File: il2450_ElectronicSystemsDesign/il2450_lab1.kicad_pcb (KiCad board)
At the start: 2 copper layers, 33 x 31.5 mm, 76 parts, among them P1 USB_OTG, P2 Spy-Bi-Wire, P3 UART, U1 LM1117-3.3, U2 MSP430G2553IPW20, U3 TMP101NA/250, Y1 Crystal

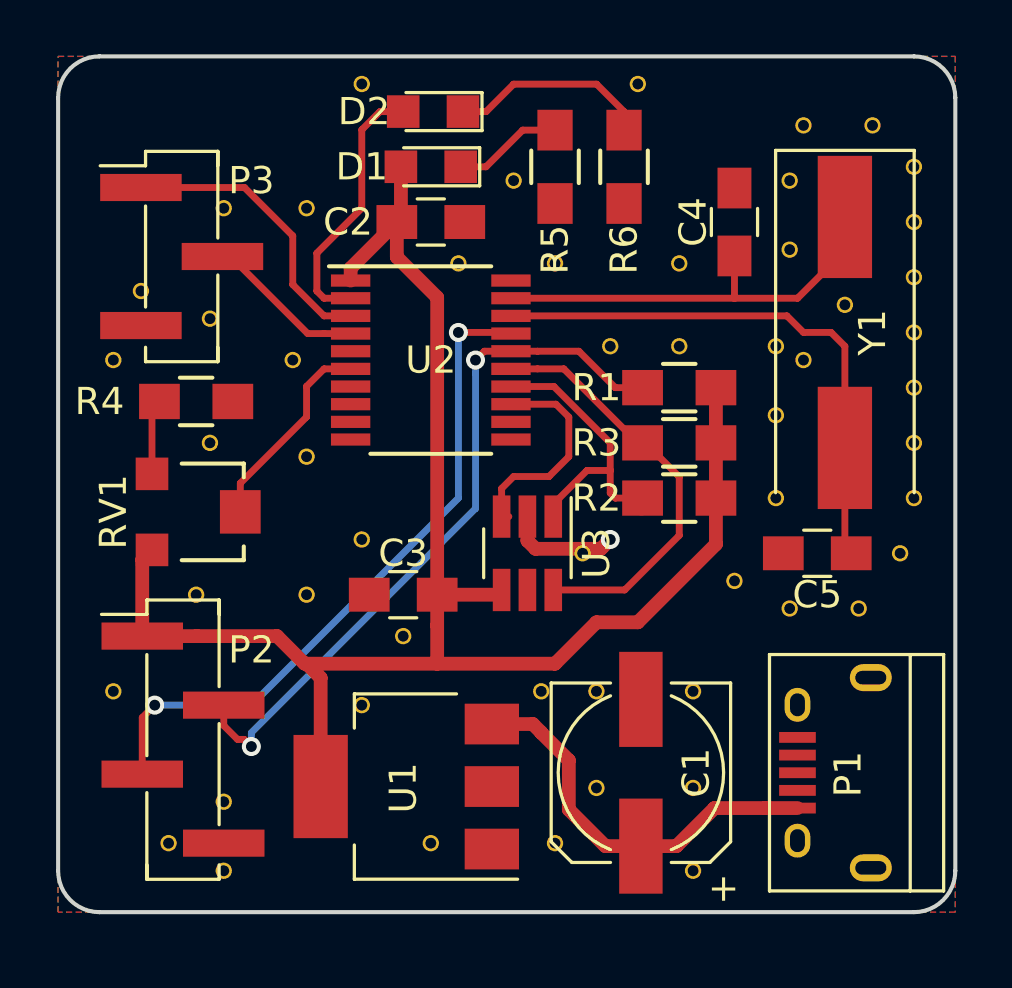
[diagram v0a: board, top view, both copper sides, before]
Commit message: Added board dimensions
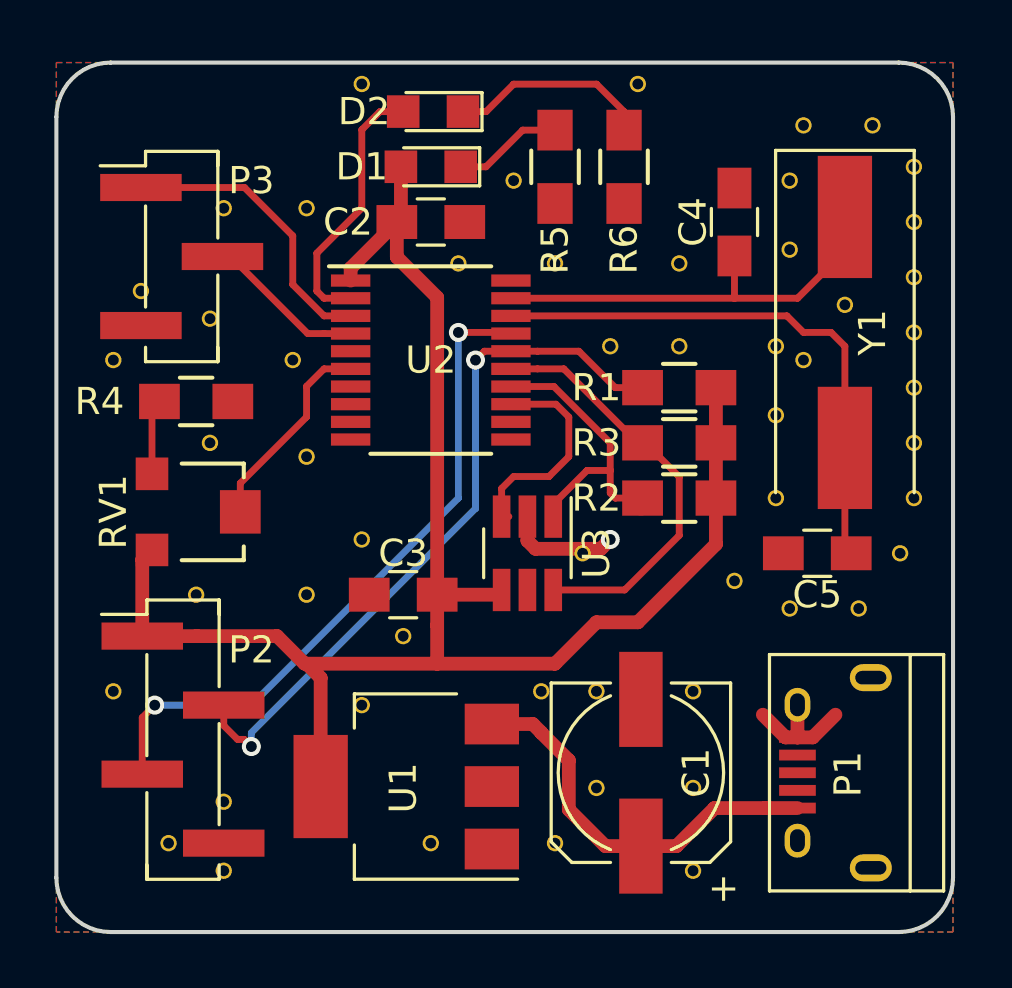
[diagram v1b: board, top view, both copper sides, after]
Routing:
- net GND: track 4.20 -> 8.77 mm
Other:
- board size 33 x 31.5 mm -> 33 x 32 mm
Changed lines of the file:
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@@
 (kicad_pcb (version 4) (host pcbnew 4.0.4-stable)
   (general
-    (links 0)
-    (no_connects 10)
-    (area 130.988999 80.696999 164.159001 112.343001)
+    (links 103)
+    (no_connects 4)
+    (area 130.924999 80.924999 164.075001 113.075001)
     (thickness 1.6)
-    (drawings 11)
-    (tracks 140)
+    (drawings 13)
+    (tracks 145)
     (zones 0)
     (modules 76)
@@
     (visible_elements 7FFFFF7F)
     (pcbplotparams
-      (layerselection 0x00030_80000001)
+      (layerselection 0x00010_00000000)
       (usegerberextensions false)
-      (excludeedgelayer true)
+      (excludeedgelayer false)
       (linewidth 0.100000)
-      (plotframeref false)
+      (plotframeref true)
       (viasonmask false)
       (mode 1)
@@
       (padsonsilk false)
       (subtractmaskfromsilk false)
-      (outputformat 1)
-      (mirror false)
-      (drillshape 1)
+      (outputformat 4)
+      (mirror true)
+      (drillshape 2)
       (scaleselection 1)
-      (outputdirectory ""))
+      (outputdirectory exports/))
   )
   (net 0 "")
@@
       (xy -0.022327 10.155298) (xy 0.008466 10.155327) (xy 0.072221 10.154895)) (layer B.SilkS) (width 0.01))
   )
+  (dimension 33 (width 0.3) (layer Dwgs.User)
+    (gr_text "33.000 mm" (at 147.5 117.35) (layer Dwgs.User)
+      (effects (font (size 1.5 1.5) (thickness 0.3)))
+    )
+    (feature1 (pts (xy 131 110) (xy 131 118.7)))
+    (feature2 (pts (xy 164 110) (xy 164 118.7)))
+    (crossbar (pts (xy 164 116) (xy 131 116)))
+    (arrow1a (pts (xy 131 116) (xy 132.126504 115.413579)))
+    (arrow1b (pts (xy 131 116) (xy 132.126504 116.586421)))
+    (arrow2a (pts (xy 164 116) (xy 162.873496 115.413579)))
+    (arrow2b (pts (xy 164 116) (xy 162.873496 116.586421)))
+  )
+  (dimension 32 (width 0.3) (layer Dwgs.User)
+    (gr_text "32.000 mm" (at 167.35 97 270) (layer Dwgs.User)
+      (effects (font (size 1.5 1.5) (thickness 0.3)))
+    )
+    (feature1 (pts (xy 160 113) (xy 168.7 113)))
+    (feature2 (pts (xy 160 81) (xy 168.7 81)))
+    (crossbar (pts (xy 166 81) (xy 166 113)))
+    (arrow1a (pts (xy 166 113) (xy 165.413579 111.873496)))
+    (arrow1b (pts (xy 166 113) (xy 166.586421 111.873496)))
+    (arrow2a (pts (xy 166 81) (xy 165.413579 82.126504)))
+    (arrow2b (pts (xy 166 81) (xy 166.586421 82.126504)))
+  )
+  (gr_arc (start 162 83) (end 162 81) (angle 90) (layer Edge.Cuts) (width 0.15))
+  (gr_arc (start 133 83) (end 131 83) (angle 90) (layer Edge.Cuts) (width 0.15))
+  (gr_arc (start 133 111) (end 133 113) (angle 90) (layer Edge.Cuts) (width 0.15))
+  (gr_arc (start 162 111) (end 164 111) (angle 90) (layer Edge.Cuts) (width 0.15))
   (gr_text "Roberts Gotlaufs 2017" (at 147.828 110.744) (layer B.SilkS)
     (effects (font (size 1.5 1.5) (thickness 0.3)) (justify mirror))
@@
     (effects (font (size 2.3 2.3) (thickness 0.4) italic) (justify mirror))
   )
-  (gr_arc (start 162.56 110.744) (end 164.084 110.744) (angle 90) (layer Edge.Cuts) (width 0.15))
-  (gr_line (start 131.064 82.296) (end 131.064 110.744) (layer Edge.Cuts) (width 0.15))
-  (gr_line (start 162.56 80.772) (end 132.588 80.772) (layer Edge.Cuts) (width 0.15))
-  (gr_line (start 164.084 110.744) (end 164.084 82.296) (layer Edge.Cuts) (width 0.15))
-  (gr_line (start 132.588 112.268) (end 162.56 112.268) (layer Edge.Cuts) (width 0.15))
-  (gr_arc (start 132.588 110.744) (end 132.588 112.268) (angle 90) (layer Edge.Cuts) (width 0.15))
-  (gr_arc (start 132.588 82.296) (end 131.064 82.296) (angle 90) (layer Edge.Cuts) (width 0.15))
-  (gr_arc (start 162.56 82.296) (end 162.56 80.772) (angle 90) (layer Edge.Cuts) (width 0.15))
+  (gr_line (start 131 83) (end 131 111) (layer Edge.Cuts) (width 0.15))
+  (gr_line (start 162 81) (end 133 81) (layer Edge.Cuts) (width 0.15))
+  (gr_line (start 164 111) (end 164 83) (layer Edge.Cuts) (width 0.15))
+  (gr_line (start 133 113) (end 162 113) (layer Edge.Cuts) (width 0.15))
   (segment (start 152.512548 109.83651) (end 153.820548 109.83651) (width 0.508) (layer F.Cu) (net 1))
   (segment (start 153.820548 109.83651) (end 155.220548 108.43651) (width 0.508) (layer F.Cu) (net 1))
@@
   (segment (start 148.844 105.664) (end 148.844 105.653962) (width 0.508) (layer F.Cu) (net 1))
   (segment (start 148.844 105.653962) (end 148.534548 105.34451) (width 0.508) (layer F.Cu) (net 1))
+  (segment (start 157.83651 105.83651) (end 157 105) (width 0.508) (layer F.Cu) (net 2))
+  (segment (start 158.274548 105.83651) (end 157.83651 105.83651) (width 0.508) (layer F.Cu) (net 2))
+  (segment (start 158.274548 105.83651) (end 158.83651 105.83651) (width 0.508) (layer F.Cu) (net 2))
+  (segment (start 158.83651 105.83651) (end 159.67302 105) (width 0.508) (layer F.Cu) (net 2))
+  (segment (start 158.274548 105.83651) (end 158.274548 104.63651) (width 0.508) (layer F.Cu) (net 2))
   (segment (start 148.336 97.71) (end 148.336 98.596522) (width 0.508) (layer F.Cu) (net 2))
   (segment (start 148.336 98.596522) (end 148.635879 98.896401) (width 0.508) (layer F.Cu) (net 2))
@@
     (polygon
       (pts
-        (xy 131.064 112.268) (xy 131.064 80.772) (xy 164.084 80.772) (xy 164.084 112.268)
+        (xy 164 113) (xy 131 113) (xy 131 81) (xy 164 81)
       )
     )
@@
     (polygon
       (pts
-        (xy 131.064 112.268) (xy 131.064 80.772) (xy 164.084 80.772) (xy 164.084 112.268)
+        (xy 164 113) (xy 131 113) (xy 131 81) (xy 164 81)
       )
     )
